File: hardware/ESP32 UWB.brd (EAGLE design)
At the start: 72 x 32.6 mm, 53 parts, among them IC1 CP2104, J2 HEADER-12P-2.54, J3 USB-MICRO-5P, Q3 S8050, Q4 S8050, U2 ME6217C33M5G, U4 LD1117/3.3v, U5 DWM1000, U6 ESP32-C3-MINI-1-N4

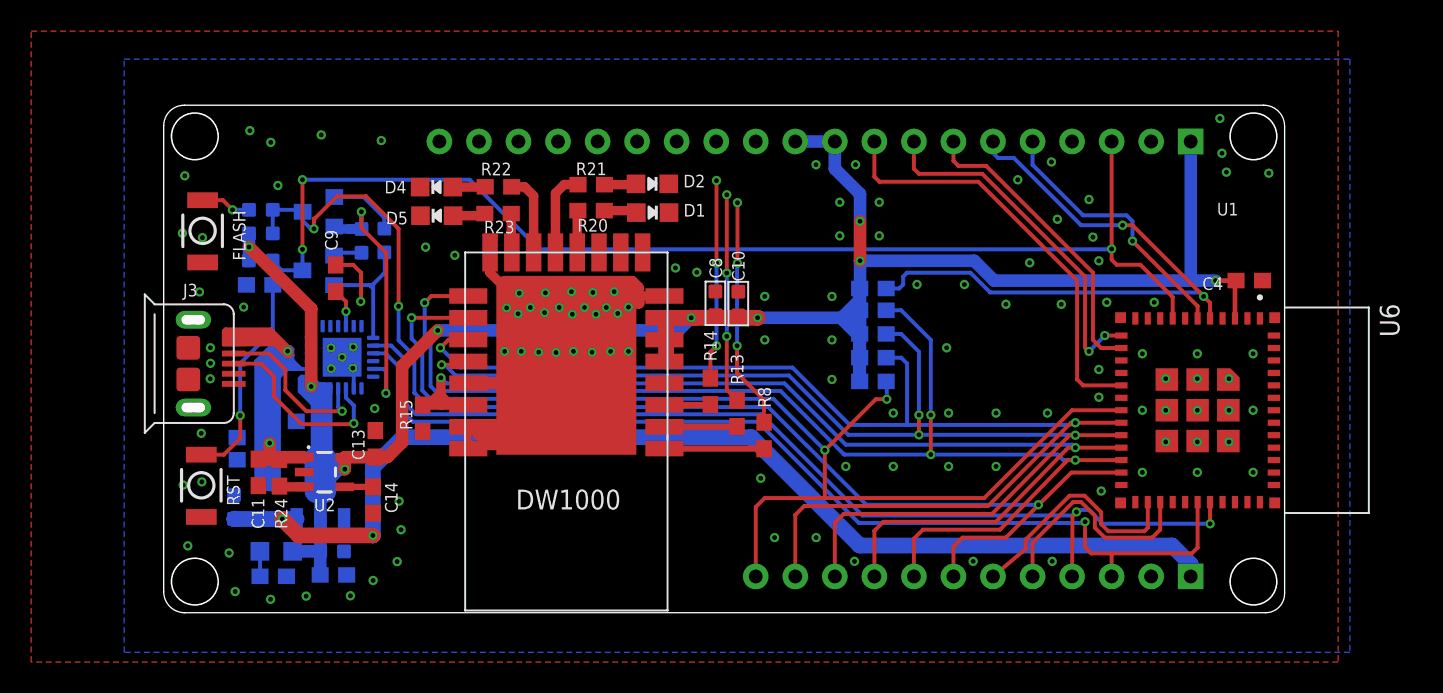
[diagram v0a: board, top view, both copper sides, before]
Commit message: switched various parts to more newer or more available part, moved all to the front
Switched Parts:
*  USB-Serial Converter CP2104 -> CP2102N
*  3.3V LDO
*  Micro USB Connector

All parts are now on the front side which means expensive double sided assembly is no longer needed.
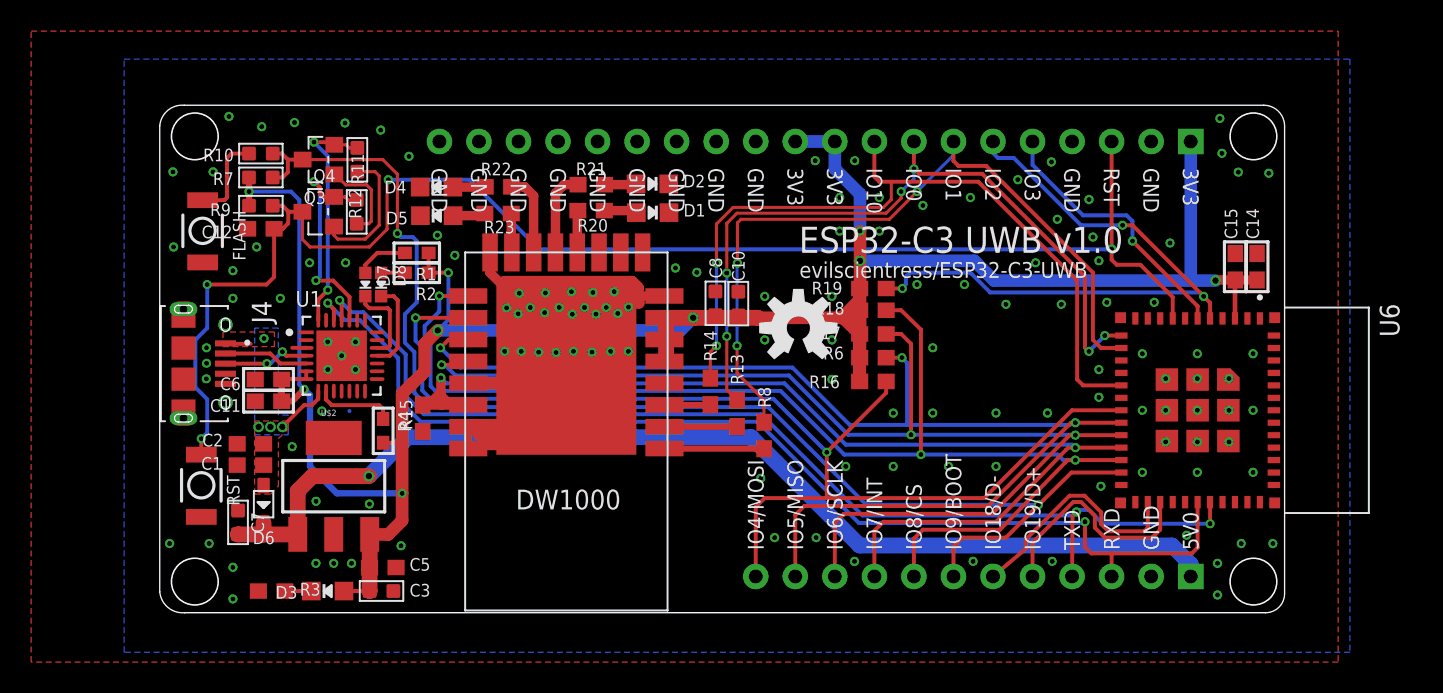
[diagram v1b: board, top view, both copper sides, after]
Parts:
- removed C13: 1.0uF, SparkFun-Capacitors:0603
- removed C4: 10uF, rcl:C0603
- removed C9: 10uf, microbuilder:0603-NO
- removed IC1: CP2104, microbuilder:QFN24_4MM_SMSC
- removed J3: USB-MICRO-5P, Connector:MICRO-USB-5P
- removed R24: 10k, SparkFun-Resistors:0603
- removed U2: ME6217C33M5G, SparkFun-IC-Power:SOT23-5
- removed U4: LD1117/3.3v, IC:SOT89
- added C15: 100n, isystems:0603
- added D7: BLUE, isystems:CHIPLED_0603_NOOUTLINE
- added D8: RED, isystems:CHIPLED_0603_NOOUTLINE
- added J4: 10118194-0001LF, 10118194-0001LF:AMPHENOL_10118194-0001LF
- added R1, R2: 470R, isystems:_0603
- added R4: 1k, isystems:_0603
- added U$2: V_REG_MIC2920, SparkFun-PowerIC:SOT223
- added U1: SILICON_LABS_CP2102N-A01-GQFN28SILICON_LABS_CP2102N-A01-GQF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, Silicon Labs - CP2102N-A01-GQFN28:SILICON_LABS_CP2102N-A01-GQFN28_3
- C11: value 1.0uF -> 4.7uF; device SparkFun-Capacitors:0603 -> isystems:0603
- C14: value NC -> 10u; device SparkFun-Capacitors:0603 -> isystems:0603
- C6: value 10uf -> 100n; device microbuilder:0603-NO -> isystems:0603
- U$1: device Logo:MAKERFABS_0.3 -> SparkFun-Aesthetics:OSHW-LOGO-M
- moved C14 58.7 mm to (70.2, 22.2), turned to 90 degrees
- moved U$1 17.8 mm to (40.8, 18.3), flipped to the top
- moved R12 5.21 mm to (12.4, 29.1), flipped to the top
- moved C11 4.62 mm to (6.73, 13.6), turned to 180 degrees
- moved D3 4.17 mm to (10.5, 1.39), flipped to the top, turned to 90 degrees
- moved C3 4.07 mm to (14.0, 1.39), flipped to the top, turned to 0 degrees
- moved C6 3.77 mm to (6.73, 15.0), flipped to the top, turned to 180 degrees
- moved Q4 3.76 mm to (9.93, 25.8), flipped to the top, turned to 90 degrees
- moved R10 3.62 mm to (6.24, 29.5), flipped to the top, turned to 0 degrees
- moved C12 3.60 mm to (6.24, 24.7), flipped to the top, turned to 180 degrees
- moved R7 3.60 mm to (6.24, 28.0), flipped to the top, turned to 180 degrees
- moved R9 3.52 mm to (6.24, 26.1), flipped to the top, turned to 180 degrees
- moved Q3 3.35 mm to (9.94, 29.1), flipped to the top, turned to 90 degrees
- moved C5 3.21 mm to (14.1, 2.91), flipped to the top, turned to 0 degrees
- moved R11 2.56 mm to (12.4, 25.7), flipped to the top, turned to 90 degrees
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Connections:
- removed net EN: R24.1, U2.3
- removed net IO27: R14.1
- removed net IO32: R13.1
- removed net IO33: R8.1
- new net N$4: D8.A, R2.2
- new net N$6: D8.C, U1.18
- new net N$8: R4.1, U1.9
- net +3V3: now also C11.1, C14.1, C15.1, R1.1, R2.1, R4.2, U$2.3, U1.6, U1.7; no longer C13.1, C4.1, IC1.5, IC1.6, IC1.7, U2.5, U4.2, U4.4
- net D+: now also J4.3, U1.4; no longer IC1.3, J3.3
- net D-: now also J4.2, U1.5; no longer IC1.4, J3.2
- net DTR: now also U1.28; no longer IC1.23
- net GND: now also C15.2, J4.5, J4.S1, J4.S2, J4.S3, J4.S4, J4.S5, J4.S6, U$2.2, U1.29, U1.3; no longer C13.2, C4.2, C9.2, IC1.2, IC1.THERM, J3.5, J3.E1, J3.E2, J3.P1, J3.P2, U2.2, U4.1
- net IO0: now also R13.1
- net IO1: now also R8.1
- net IO10: now also R14.1
- net N$2: now also D7.A, R1.2; no longer C9.1, IC1.16
- net N$3: now also D7.C, U1.19; no longer C14.1, U2.4
- net RTS: now also U1.24; no longer IC1.19
- net RXD: now also U1.26; no longer IC1.21
- net TXD: now also U1.25; no longer IC1.20
- net VBUS: now also J4.1, U1.8; no longer C11.1, IC1.8, J3.1, R24.2, U2.1
- net VDD5V: now also U$2.1; no longer U4.3
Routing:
- net VBUS: track 95.1 -> 5.17 mm, vias 2 -> 4
- net IO1: track 19.5 -> 49.6 mm, vias 0 -> 3
- net IO0: track 23.0 -> 48.8 mm, vias 2 -> 6
- net IO10: track 27.4 -> 50.5 mm, vias 0 -> 2
- net IO33: track 15.0 -> 0.00 mm, vias 3 -> 0
- net IO32: track 13.5 -> 0.00 mm, vias 3 -> 0
- net IO27: track 12.9 -> 0.00 mm, vias 3 -> 0
- net D+: track 12.5 -> 5.61 mm, vias 1 -> 2
- net N$13: track 1.84 -> 8.63 mm
- net +3V3: track 194.6 -> 188.6 mm
- net N$6: track 0.00 -> 5.77 mm
- net RXD: track 65.4 -> 70.9 mm, vias 1 -> 2
- net RTS: track 8.66 -> 14.2 mm, vias 0 -> 2
- net D-: track 10.8 -> 5.45 mm, vias 1 -> 0
- net GND: track 46.5 -> 41.3 mm, vias 124 -> 134
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- added copper zone on layer 1, net VBUS
- added copper zone on layer 16, net VBUS
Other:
- board size 72 x 32.6 mm -> 72.3 x 32.6 mm
- board text added: "ESP32-C3 UWB v1.0"
- board text added: "IO10"
- board text added: "IO18/D-"
- board text added: "IO19/D+"
- board text added: "IO4/MOSI"
- board text added: "IO5/MISO"
- board text added: "IO6/SCLK"
- board text added: "IO7/INT"
- board text added: "IO8/CS"
- board text added: "IO9/BOOT"
- board text added: "RXD"
- board text added: "TXD"
- board text added: "evilscientress/ESP32-C3-UWB"
- board text removed: "ESP32 UWB v1.0"
- board text removed: "IO12"
- board text removed: "IO13"
- board text removed: "IO14"
- board text removed: "IO15"
- board text removed: "IO16"
- board text removed: "IO17"
- board text removed: "IO18"
- board text removed: "IO19"
- board text removed: "IO21"
- board text removed: "IO22"
- board text removed: "IO23"
- board text removed: "IO25"
- board text removed: "IO26"
- board text removed: "IO27"
- board text removed: "IO32"
- board text removed: "IO33"
- board text removed: "IO34"
- board text removed: "IO35"
- board text removed: "IO36"
- board text removed: "IO39"
- board text removed: "IO4"
- board text removed: "IO5"
- board text removed: "U1"
- board text removed: "www.makerfabs.com"

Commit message: switched resistor and capacitor footprints, placed labels
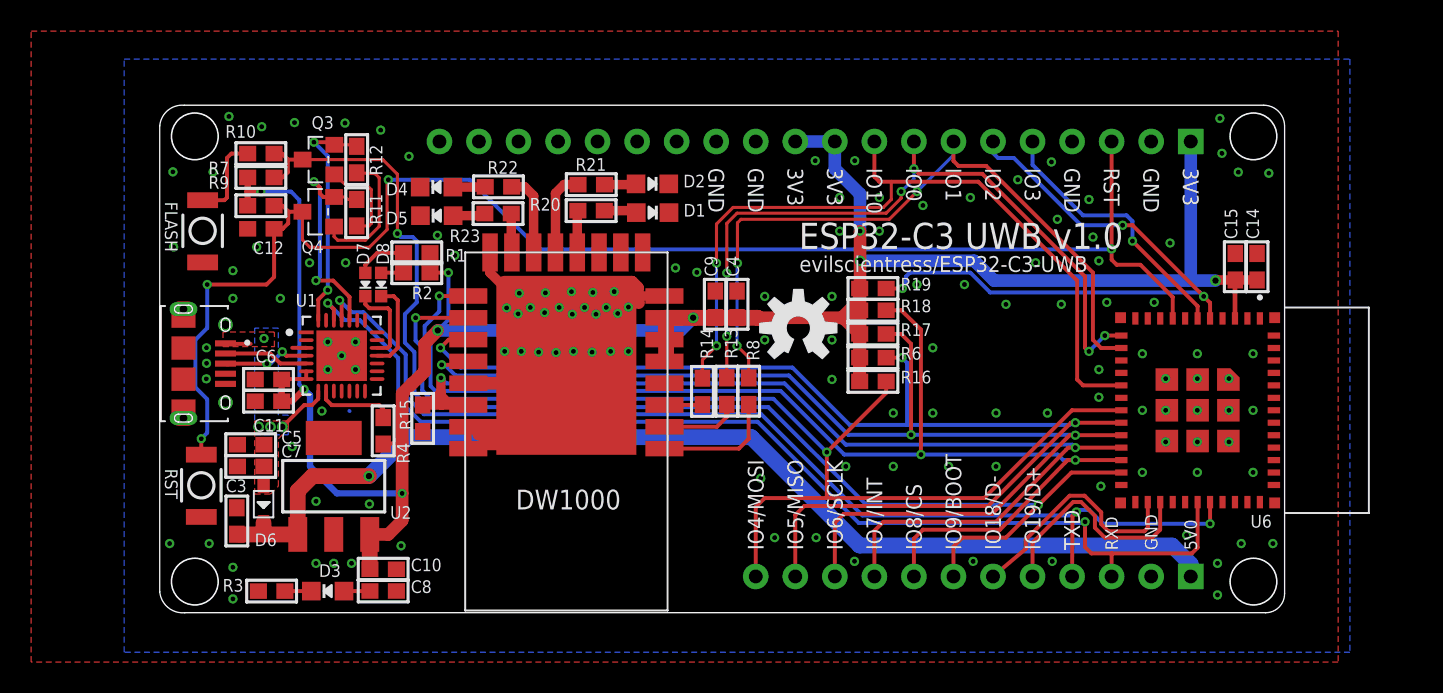
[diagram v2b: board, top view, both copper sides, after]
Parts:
- removed C1: 10uf, microbuilder:0603-NO
- removed C2: 100nf, microbuilder:0603-NO
- added C4: 10u, isystems:0603
- added C9: 100n, isystems:0603
- C10: value 0.1uF -> 100n; device Discrete:C0603 -> isystems:0603
- C3: value 10uF -> 10uF/16V; device Discrete:C0603 -> isystems:0603
- C5: value 10uf -> 10u; device microbuilder:0603-NO -> isystems:0603
- C7: value 10uF/16V -> 100n; device Discrete:C0603 -> isystems:0603
- C8: value 10uF -> 10u; device Discrete:C0603 -> isystems:0603
- R1, R2, R4: device isystems:_0603 -> isystems:0603
- R10, R11, R12, R7, R9: device Discrete:0603 -> isystems:0603
- R13, R14, R15, R16, R17, R18, R19, R20, R21, R22, R23, R3, R6, R8: device microbuilder:0603-NO -> isystems:0603
- moved C10 28.5 mm to (14.1, 2.79), turned to 0 degrees
- moved C8 28.2 mm to (14.1, 1.40), turned to 0 degrees
- moved C5 11.6 mm to (5.59, 10.8), turned to 180 degrees
- moved C3 10.3 mm to (4.70, 5.89), turned to 90 degrees
- moved C7 3.68 mm to (5.59, 9.40), turned to 180 degrees
- moved R8 3.01 mm to (37.6, 14.2)
- moved R13 1.57 mm to (36.2, 14.2)
- moved R14 0.51 mm to (34.6, 14.2)
- moved R11 0.05 mm to (12.4, 25.7)
- renumbered U$2 to U2
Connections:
- net +3V3: now also C4.1, C9.1; no longer C3.1, C5.1
- net GND: now also C4.2, C9.2; no longer C1.2, C2.2
- net VBUS: now also C5.1, C7.1; no longer C1.1, C2.1
- net VDD5V: now also C3.1; no longer C7.1
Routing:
- net IO1: track 49.6 -> 46.4 mm
- net +3V3: track 188.6 -> 186.5 mm
- net IO0: track 48.8 -> 47.1 mm
- net N$10: track 6.65 -> 7.88 mm
- net N$12: track 2.97 -> 2.46 mm
